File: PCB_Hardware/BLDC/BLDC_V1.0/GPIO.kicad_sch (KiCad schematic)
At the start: 16 parts, among them J8 Conn_02x06_Odd_Even, J9 Conn_01x06_Socket, Q12 BSS84, U14 SRV05-4, U15 TS5A3159ADBVR, U8 SRV05-4, U9 SRV05-4

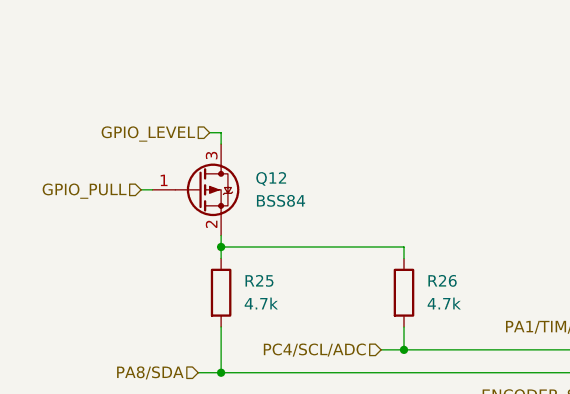
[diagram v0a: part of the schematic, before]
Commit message: foget to add the GPIO to change the voltage for AUX2 SPI port, removed the ability to pull AUX pins down to free a pin
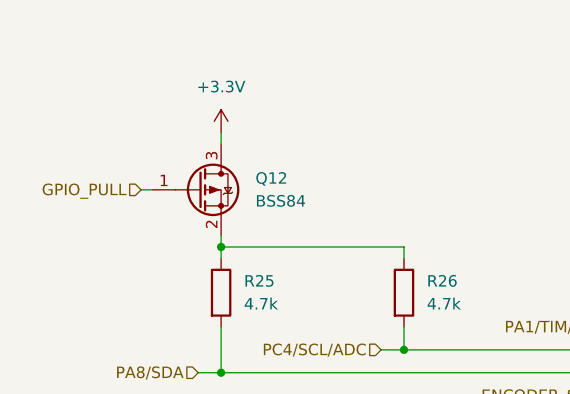
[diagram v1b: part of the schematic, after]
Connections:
- net GPIO_LEVEL is gone; now on net +3.3V: Q12.3 (D)
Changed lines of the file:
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@@
 	(wire
 		(pts
-			(xy 67.31 31.75) (xy 68.58 31.75)
-		)
-		(stroke
-			(width 0)
-			(type default)
-		)
-	)
-	(wire
-		(pts
 			(xy 127 142.24) (xy 162.56 142.24)
 		)
@@
 	(wire
 		(pts
+			(xy 68.58 31.75) (xy 68.58 33.02)
+		)
+		(stroke
+			(width 0)
+			(type default)
+		)
+	)
+	(wire
+		(pts
 			(xy 127 139.7) (xy 132.08 139.7)
 		)
@@
 	(wire
 		(pts
-			(xy 68.58 31.75) (xy 68.58 33.02)
-		)
-		(stroke
-			(width 0)
-			(type default)
-		)
-	)
-	(wire
-		(pts
 			(xy 172.72 25.4) (xy 172.72 26.67)
 		)
@@
 		)
 	)
-	(hierarchical_label "GPIO_LEVEL"
-		(shape input)
-		(at 67.31 31.75 180)
-		(effects
-			(font
-				(size 1.27 1.27)
-			)
-			(justify right)
-		)
-	)
 	(hierarchical_label "PC4{slash}SCL{slash}ADC"
 		(shape input)
@@
 					(unit 1)
 				)
+			)
+		)
+	)
+	(symbol
+		(lib_id "power:+3.3V")
+		(at 68.58 31.75 0)
+		(unit 1)
+		(body_style 1)
+		(exclude_from_sim no)
+		(in_bom yes)
+		(on_board yes)
+		(in_pos_files yes)
+		(dnp no)
+		(fields_autoplaced yes)
+		(property "Reference" "#PWR070"
+			(at 68.58 35.56 0)
+			(hide yes)
+			(show_name no)
+			(do_not_autoplace no)
+			(effects
+				(font
+					(size 1.27 1.27)
+				)
+			)
+		)
+		(property "Value" "+3.3V"
+			(at 68.58 26.67 0)
+			(show_name no)
+			(do_not_autoplace no)
+			(effects
+				(font
+					(size 1.27 1.27)
+				)
+			)
+		)
+		(property "Footprint" ""
+			(at 68.58 31.75 0)
+			(hide yes)
+			(show_name no)
+			(do_not_autoplace no)
+			(effects
+				(font
+					(size 1.27 1.27)
+				)
+			)
+		)
+		(property "Datasheet" ""
+			(at 68.58 31.75 0)
+			(hide yes)
+			(show_name no)
+			(do_not_autoplace no)
+			(effects
+				(font
+					(size 1.27 1.27)
+				)
+			)
+		)
+		(property "Description" "Power symbol creates a global label with name \"+3.3V\""
+			(at 68.58 31.75 0)
+			(hide yes)
+			(show_name no)
+			(do_not_autoplace no)
+			(effects
+				(font
+					(size 1.27 1.27)
+				)
+			)
+		)
+		(pin "1"
+		)
+		(instances
+			(project "BLDC_V1.0"
+				(path "/55f9ea03-7b89-4b61-9599-7cac20295fbb/4ed90f4a-9319-42f4-aa74-161824698181"
+					(reference "#PWR070")
+					(unit 1)
+				)
